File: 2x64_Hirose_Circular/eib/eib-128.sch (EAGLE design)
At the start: 12 parts

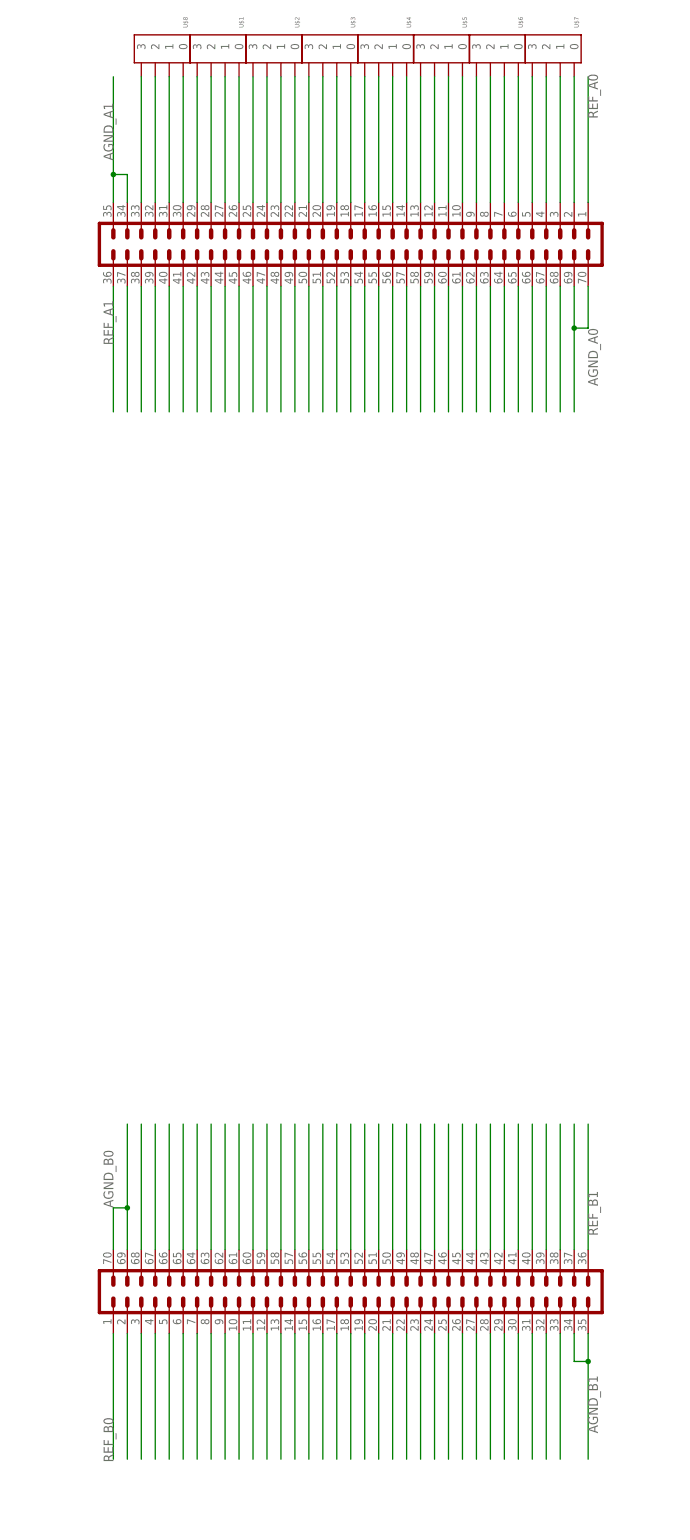
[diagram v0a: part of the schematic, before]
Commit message: Started 128 channel EIB layout.
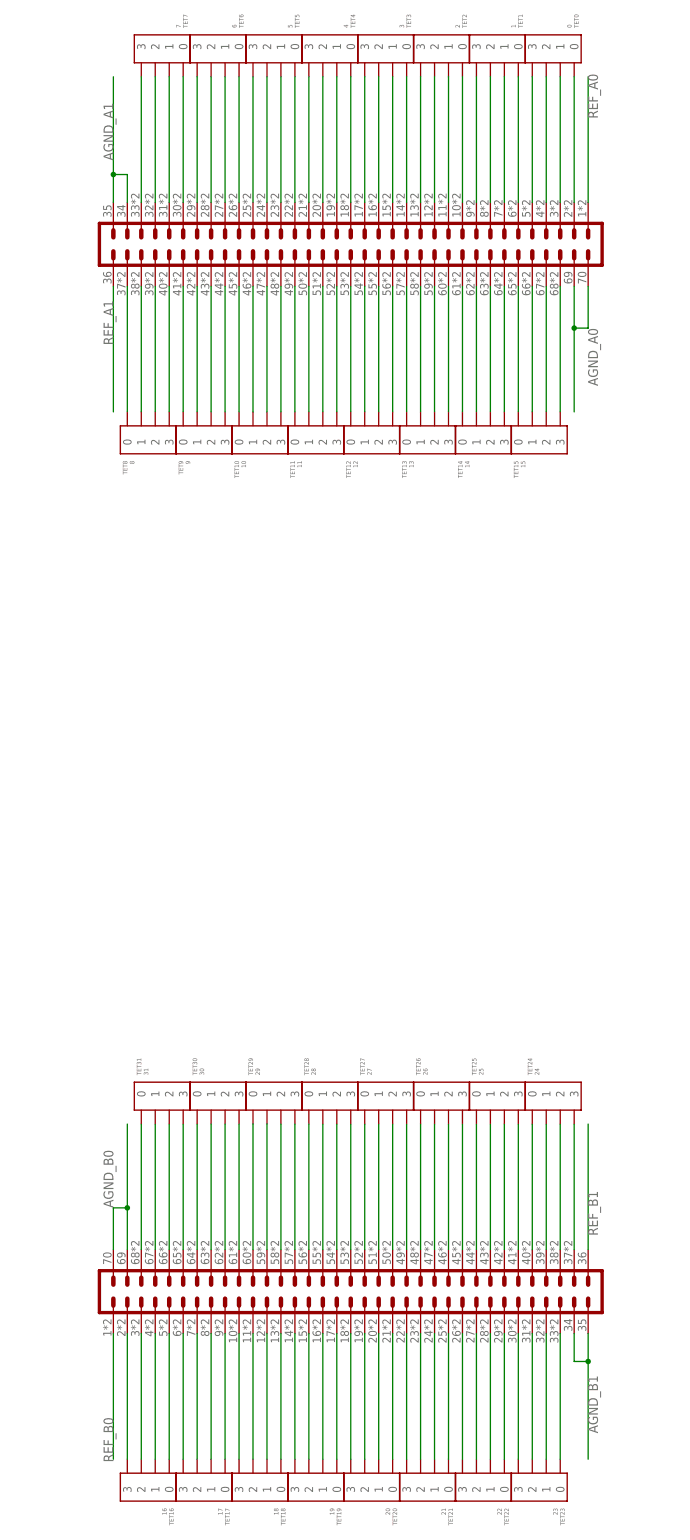
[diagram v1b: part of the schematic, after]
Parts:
- removed U$1, U$2, U$3, U$4, U$5, U$6, U$7, U$8: (no value), jonnew:TETRODE_0.5ID_0.7OD
- added TET0: 0, jonnew:TETRODE_128_0.5ID_0.7OD
- added TET1: 1, jonnew:TETRODE_128_0.5ID_0.7OD
- added TET10: 10, jonnew:TETRODE_128_0.5ID_0.7OD
- added TET11: 11, jonnew:TETRODE_128_0.5ID_0.7OD
- added TET12: 12, jonnew:TETRODE_128_0.5ID_0.7OD
- added TET13: 13, jonnew:TETRODE_128_0.5ID_0.7OD
- added TET14: 14, jonnew:TETRODE_128_0.5ID_0.7OD
- added TET15: 15, jonnew:TETRODE_128_0.5ID_0.7OD
- added TET16: 16, jonnew:TETRODE_128_0.5ID_0.7OD
- added TET17: 17, jonnew:TETRODE_128_0.5ID_0.7OD
- added TET18: 18, jonnew:TETRODE_128_0.5ID_0.7OD
- added TET19: 19, jonnew:TETRODE_128_0.5ID_0.7OD
- added TET2: 2, jonnew:TETRODE_128_0.5ID_0.7OD
- added TET20: 20, jonnew:TETRODE_128_0.5ID_0.7OD
- added TET21: 21, jonnew:TETRODE_128_0.5ID_0.7OD
- added TET22: 22, jonnew:TETRODE_128_0.5ID_0.7OD
- added TET23: 23, jonnew:TETRODE_128_0.5ID_0.7OD
- added TET24: 24, jonnew:TETRODE_128_0.5ID_0.7OD
- added TET25: 25, jonnew:TETRODE_128_0.5ID_0.7OD
- added TET26: 26, jonnew:TETRODE_128_0.5ID_0.7OD
- added TET27: 27, jonnew:TETRODE_128_0.5ID_0.7OD
- added TET28: 28, jonnew:TETRODE_128_0.5ID_0.7OD
- added TET29: 29, jonnew:TETRODE_128_0.5ID_0.7OD
- added TET3: 3, jonnew:TETRODE_128_0.5ID_0.7OD
- added TET30: 30, jonnew:TETRODE_128_0.5ID_0.7OD
- added TET31: 31, jonnew:TETRODE_128_0.5ID_0.7OD
- added TET4: 4, jonnew:TETRODE_128_0.5ID_0.7OD
- added TET5: 5, jonnew:TETRODE_128_0.5ID_0.7OD
- added TET6: 6, jonnew:TETRODE_128_0.5ID_0.7OD
- added TET7: 7, jonnew:TETRODE_128_0.5ID_0.7OD
- added TET8: 8, jonnew:TETRODE_128_0.5ID_0.7OD
- added TET9: 9, jonnew:TETRODE_128_0.5ID_0.7OD
- A, B: device jonnew:PINHD-2X35_DF40HEAD -> jonnew:PINHD-2X35_DF40HEAD-EIB
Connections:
- net N$100: now also TET25.2
- net N$1000: now also TET8.0
- net N$101: now also TET25.1
- net N$102: now also TET25.0
- net N$103: now also TET26.3
- net N$104: now also TET26.2
- net N$105: now also TET26.1
- net N$106: now also TET26.0
- net N$107: now also TET27.3
- net N$108: now also TET27.2
- net N$109: now also TET27.1
- net N$110: now also TET27.0
- net N$111: now also TET28.3
- net N$112: now also TET28.2
- net N$113: now also TET28.1
- net N$114: now also TET28.0
- net N$115: now also TET29.3
- net N$116: now also TET29.2
- net N$117: now also TET29.1
- net N$118: now also TET29.0
- net N$119: now also TET30.3
- net N$120: now also TET30.2
- net N$121: now also TET30.1
- net N$122: now also TET30.0
- net N$123: now also TET31.3
- net N$124: now also TET31.2
- net N$125: now also TET31.1
- net N$126: now also TET31.0
- net N$127: now also TET16.3
- net N$128: now also TET24.3
- net N$199: now also TET7.3; no longer U$8.3
- net N$200: now also TET7.2; no longer U$8.2
- net N$201: now also TET7.1; no longer U$8.1
- net N$202: now also TET7.0; no longer U$8.0
- net N$203: now also TET6.3; no longer U$1.3
- net N$204: now also TET6.2; no longer U$1.2
- net N$205: now also TET6.1; no longer U$1.1
- net N$206: now also TET6.0; no longer U$1.0
- net N$207: now also TET5.3; no longer U$2.3
- net N$208: now also TET5.2; no longer U$2.2
- net N$209: now also TET5.1; no longer U$2.1
- net N$210: now also TET5.0; no longer U$2.0
- net N$211: now also TET4.3; no longer U$3.3
- net N$212: now also TET4.2; no longer U$3.2
- net N$213: now also TET4.1; no longer U$3.1
- net N$214: now also TET4.0; no longer U$3.0
- net N$215: now also TET3.3; no longer U$4.3
- net N$216: now also TET3.2; no longer U$4.2
- net N$217: now also TET3.1; no longer U$4.1
- net N$218: now also TET3.0; no longer U$4.0
- net N$219: now also TET2.3; no longer U$5.3
- net N$220: now also TET2.2; no longer U$5.2
- net N$221: now also TET2.1; no longer U$5.1
- net N$222: now also TET2.0; no longer U$5.0
- net N$223: now also TET1.3; no longer U$6.3
- net N$224: now also TET1.2; no longer U$6.2
- net N$225: now also TET1.1; no longer U$6.1
- net N$226: now also TET1.0; no longer U$6.0
- net N$227: now also TET0.3; no longer U$7.3
- net N$228: now also TET0.2; no longer U$7.2
- net N$229: now also TET0.1; no longer U$7.1
- net N$230: now also TET0.0; no longer U$7.0
- net N$231: now also TET8.1
- net N$232: now also TET8.2
- net N$233: now also TET8.3
- net N$234: now also TET9.0
- net N$235: now also TET9.1
- net N$236: now also TET9.2
- net N$237: now also TET9.3
- net N$238: now also TET10.0
- net N$239: now also TET10.1
- net N$240: now also TET10.2
- net N$241: now also TET10.3
- net N$242: now also TET11.0
- net N$243: now also TET11.1
- net N$244: now also TET11.2
- net N$245: now also TET11.3
- net N$246: now also TET12.0
- net N$247: now also TET12.1
- net N$248: now also TET12.2
- net N$249: now also TET12.3
- net N$250: now also TET13.0
- net N$251: now also TET13.1
- net N$252: now also TET13.2
- net N$253: now also TET13.3
- net N$254: now also TET14.0
- net N$255: now also TET14.1
- net N$256: now also TET14.2
- net N$257: now also TET14.3
- net N$258: now also TET15.0
- net N$259: now also TET15.1
- net N$260: now also TET15.2
- net N$261: now also TET15.3
- net N$65: now also TET23.0
- net N$66: now also TET23.1
- net N$67: now also TET23.2
- net N$68: now also TET23.3
- net N$69: now also TET22.0
- net N$70: now also TET22.1
- net N$71: now also TET22.2
- net N$72: now also TET22.3
- net N$73: now also TET21.0
- net N$74: now also TET21.1
- net N$75: now also TET21.2
- net N$76: now also TET21.3
- net N$77: now also TET20.0
- net N$78: now also TET20.1
- net N$79: now also TET20.2
- net N$80: now also TET20.3
- net N$81: now also TET19.0
- net N$82: now also TET19.1
- net N$83: now also TET19.2
- net N$84: now also TET19.3
- net N$85: now also TET18.0
- net N$86: now also TET18.1
- net N$87: now also TET18.2
- net N$88: now also TET18.3
- net N$89: now also TET17.0
- net N$90: now also TET17.1
- net N$91: now also TET17.2
- net N$92: now also TET17.3
- net N$93: now also TET16.0
- net N$94: now also TET16.1
- net N$95: now also TET16.2
- net N$96: now also TET24.2
- net N$97: now also TET24.1
- net N$98: now also TET24.0
- net N$99: now also TET25.3

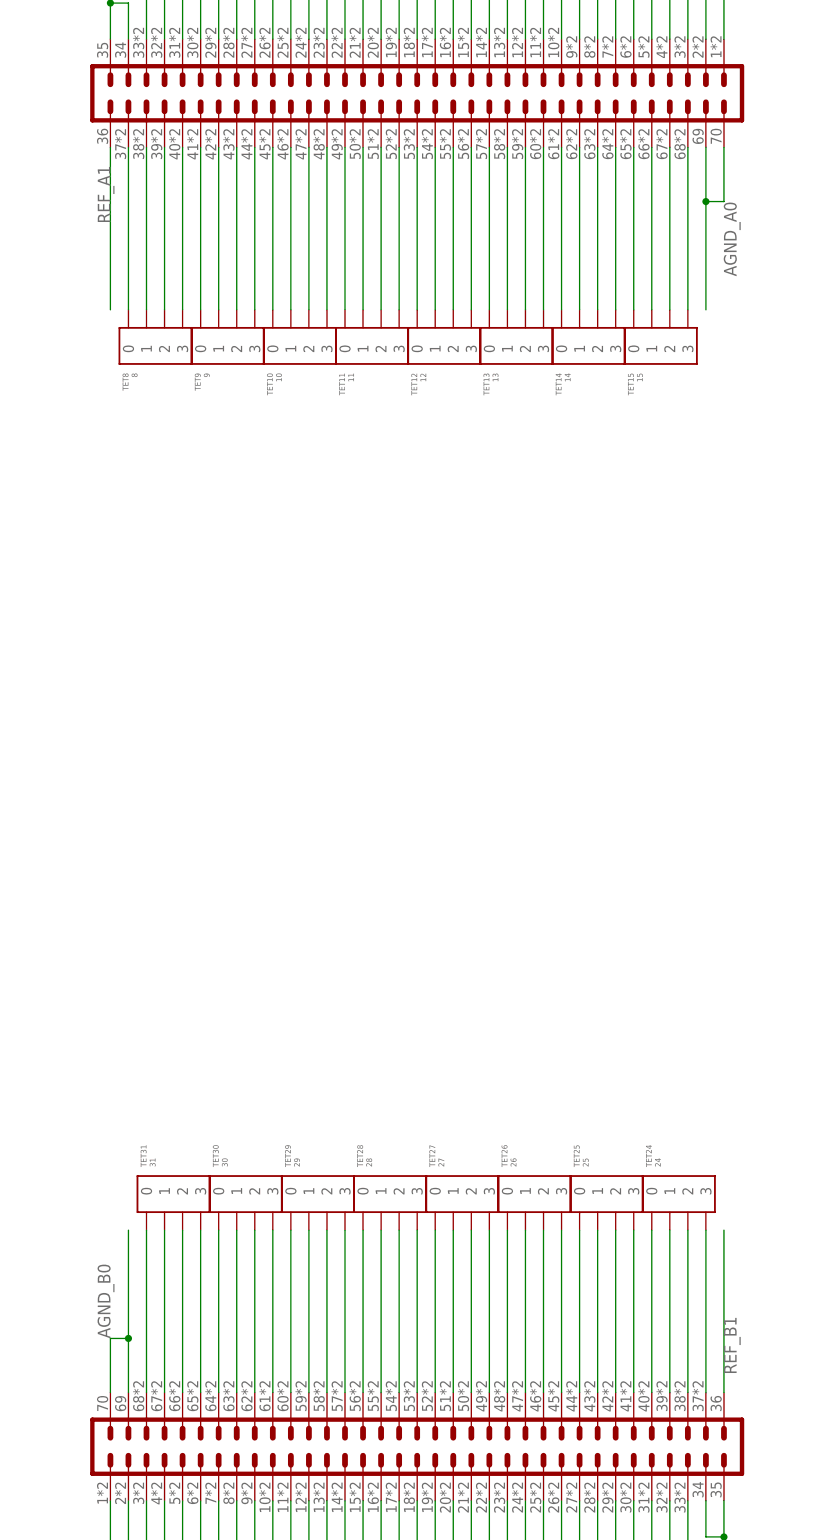
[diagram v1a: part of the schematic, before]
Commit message: Working through 128 chan EIB routing.
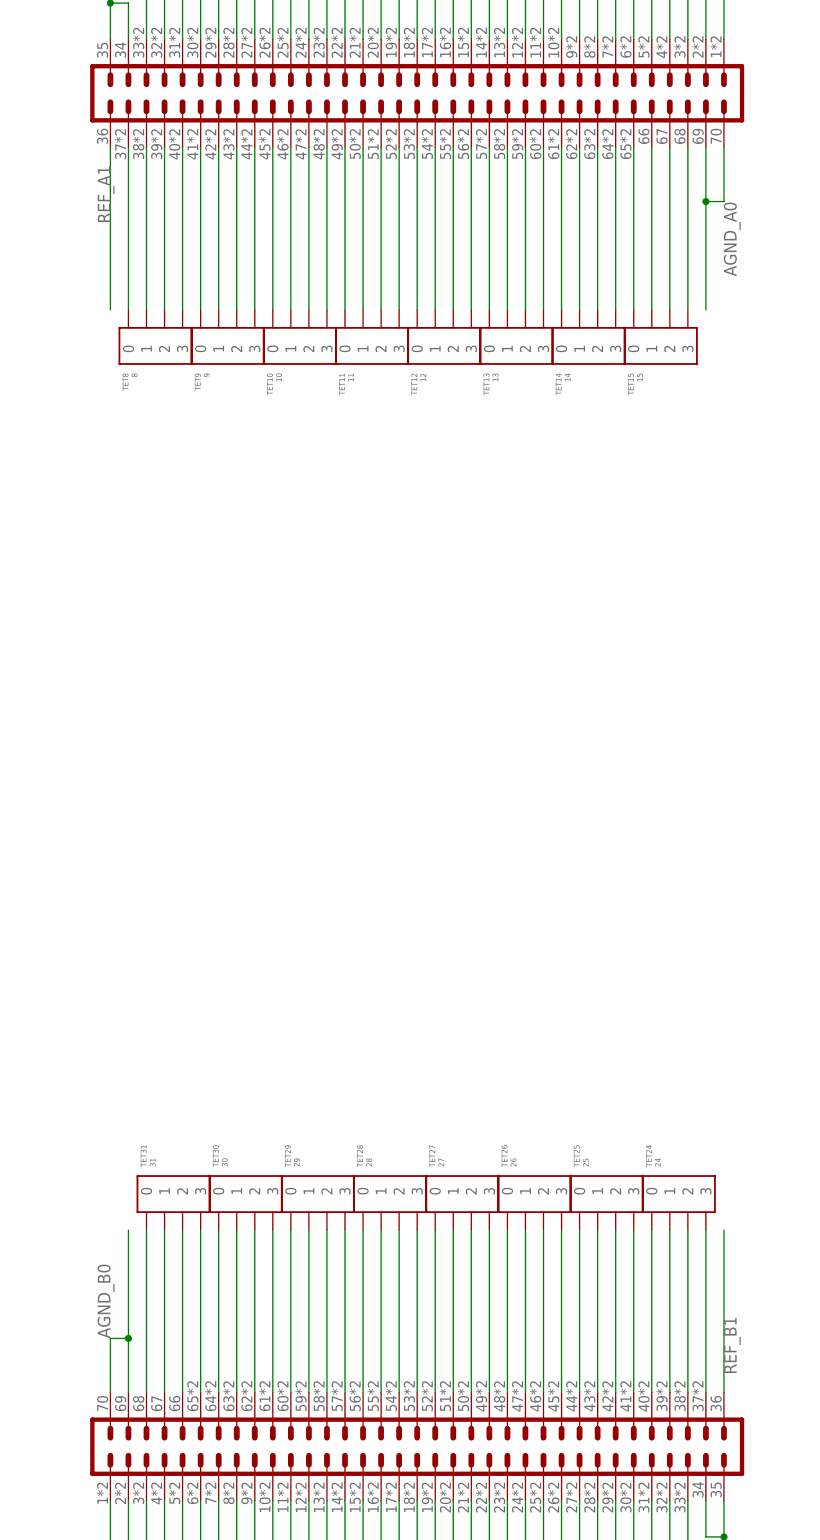
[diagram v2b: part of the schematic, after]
